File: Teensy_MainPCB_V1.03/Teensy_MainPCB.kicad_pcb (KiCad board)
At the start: 2 copper layers, 141.9 x 100 mm, 68 parts, among them J1 ODO_Right, J10 Sonar_R, J11 Cutter, J12 Sonar_L, J13 P_Right, J14 Buzzer, J15 Button, J16 Power_PCB1, J17 Power_PCB2, J18 Free01_02, J19 P_Left, J2 I2C2_0, J20 Can3, J21 Ser5, J22 FreeA16_A17, J23 ESP RFID1, J24 ESP RFID2, J25 5V IN, J26 ESP32 I2C, J27 ESP32 Sens1, J28 ESP32 FREE, J29 3.3V IN, J3 I2C0_0, J30 I2C1_0, J31 Ser3, J32 ESP32 Sens2, J33 ESP32 I2C/SER, J34 Teensy On/Off, J4 I2C1_1, J5 Bumper, J6 ODO_Left, J7 Motor_Right1, J8 Motor_Left1, J9 Rain, U2 GY-521, U3 Teensy4.1, U4 ESP32-DEVKIT-V1

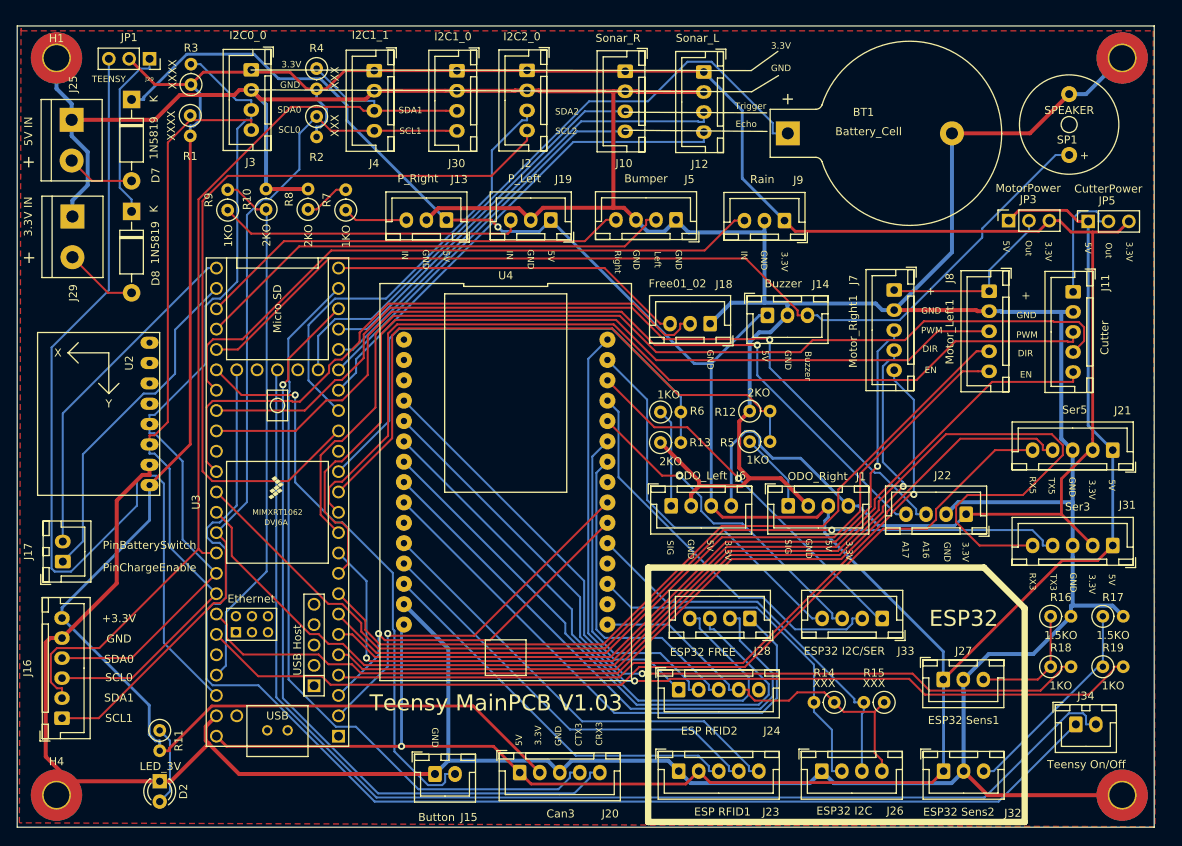
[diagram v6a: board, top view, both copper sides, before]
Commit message: Removed unused
Remove unused Items and sorting new
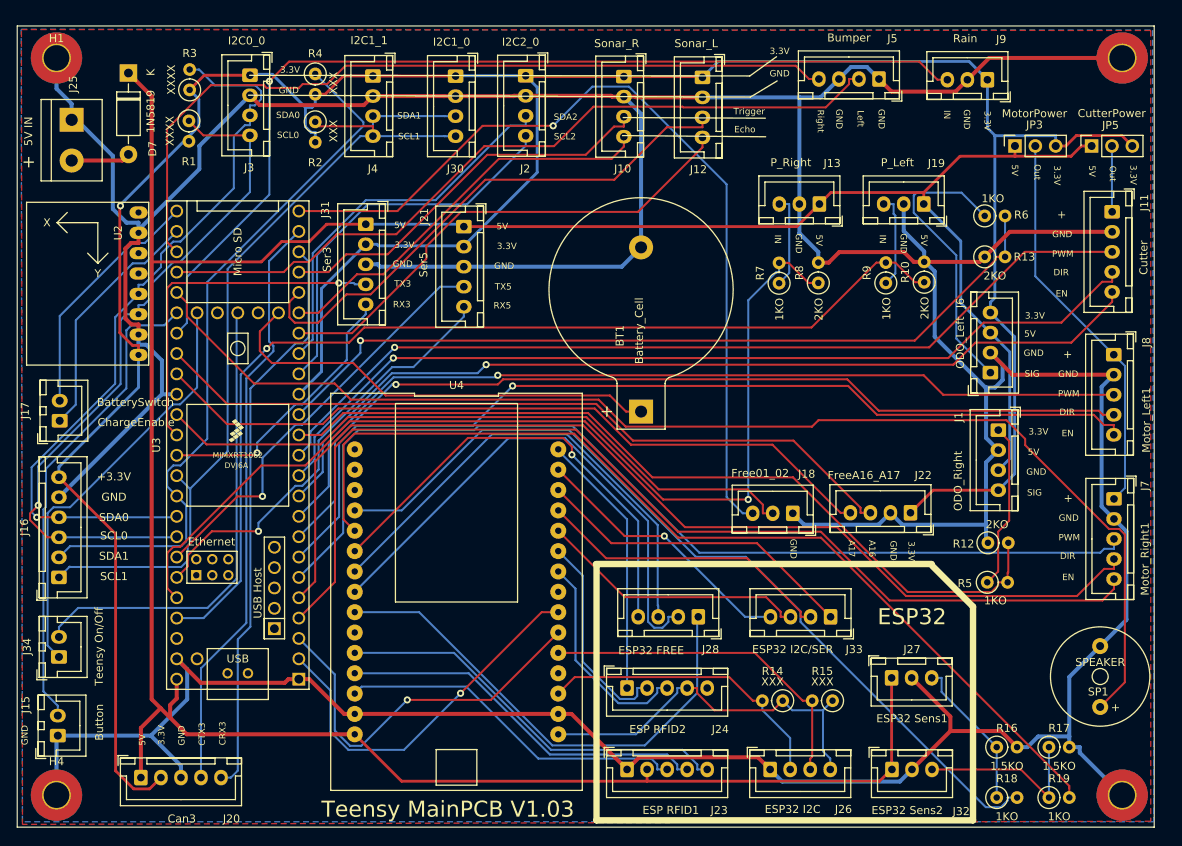
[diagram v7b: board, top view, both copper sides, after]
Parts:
- removed D2: LED_3V, LED_THT:LED_D3.0mm
- removed D8: 1N5819, Diode_THT:D_DO-41_SOD81_P10.16mm_Horizontal
- removed J14: Buzzer, Connector_JST:JST_XH_B3B-XH-A_1x03_P2.50mm_Vertical
- removed J29: 3.3V IN, TerminalBlock:TerminalBlock_bornier-2_P5.08mm
- removed JP1: Jumper_3.3V, Connector_PinSocket_2.54mm:PinSocket_1x03_P2.54mm_Vertical
- removed R11: 100, Resistor_THT:R_Axial_DIN0207_L6.3mm_D2.5mm_P2.54mm_Vertical
- moved J34 127.2 mm to (43.3, 112.8), turned to 90 degrees
- moved J31 101.5 mm to (81.6, 58.8), turned to 270 degrees
- moved J21 85.7 mm to (93.8, 59.0), turned to 270 degrees
- moved R10 82.6 mm to (151.3, 66.0)
- moved R9 82.6 mm to (146.5, 66.1)
- moved SP1 69.0 mm to (173.3, 115.2)
- moved R8 64.3 mm to (138.1, 66.1)
- moved R7 54.8 mm to (133.2, 66.1)
- moved J15 47.3 mm to (43.2, 122.6), turned to 90 degrees
- moved R6 47.3 mm to (158.8, 57.7)
- moved J20 47.3 mm to (53.5, 127.8)
- moved R13 46.6 mm to (158.8, 62.8)
- moved J19 46.6 mm to (151.2, 56.2)
- moved J13 46.6 mm to (138.2, 56.2)
- moved J6 43.2 mm to (159.6, 77.3), turned to 90 degrees
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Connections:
- J24 pad 5: Net-(J24-Pad5) -> (no net)
- R7 pad 2: Net-(R7-Pad2) -> pinPerimeterRight
- R8 pad 1: Net-(R7-Pad2) -> pinPerimeterRight
- U2 pad 5: Net-(U2-Pad5) -> (no net)
- U2 pad 6: Net-(U2-Pad6) -> (no net)
- U2 pad 7: Net-(U2-Pad7) -> GND
- U2 pad 8: Net-(U2-Pad8) -> (no net)
- U3 pad 1: Net-(U3-Pad1) -> GND
- U3 pad 15: Net-(U3-Pad15) -> +3V3
- U3 pad 34: Net-(U3-Pad34) -> GND
- U3 pad 46: Net-(JP1-Pad3) -> (no net)
- U3 pad 49: Net-(U3-Pad49) -> (no net)
- U3 pad 51: Net-(U3-Pad51) -> (no net)
- U3 pad 53: Net-(U3-Pad53) -> (no net)
- U3 pad 55: Net-(U3-Pad55) -> (no net)
- U3 pad 56: Net-(U3-Pad56) -> (no net)
- U3 pad 57: Net-(U3-Pad57) -> (no net)
- U3 pad 58: Net-(U3-Pad58) -> (no net)
- U3 pad 59: Net-(U3-Pad59) -> (no net)
- U3 pad 60: Net-(U3-Pad60) -> (no net)
- U3 pad 61: Net-(U3-Pad61) -> (no net)
- U3 pad 62: Net-(U3-Pad62) -> (no net)
- U3 pad 63: Net-(U3-Pad63) -> (no net)
- U3 pad 64: Net-(U3-Pad64) -> (no net)
- U3 pad 65: Net-(U3-Pad65) -> (no net)
- U3 pad 66: Net-(U3-Pad66) -> (no net)
- U3 pad 67: Net-(U3-Pad67) -> (no net)
- U4 pad 1: Net-(U4-Pad1) -> (no net)
- U4 pad 10: Net-(U4-Pad10) -> (no net)
- U4 pad 17: Net-(U4-Pad17) -> GND
- U4 pad 19: Net-(U4-Pad19) -> (no net)
- U4 pad 2: Net-(U4-Pad2) -> (no net)
- U4 pad 23: Net-(U4-Pad23) -> (no net)
- U4 pad 3: Net-(U4-Pad3) -> (no net)
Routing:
- net pinPerimeterRight: track 0.00 -> 126.7 mm, vias 0 -> 1
- net RX3: track 158.7 -> 34.8 mm, vias 0 -> 1
- net Net-(JP1-Pad3): track 117.0 -> 0.00 mm
- net Net-(J34-Pad1): track 162.5 -> 53.0 mm
- net Net-(J34-Pad2): track 153.9 -> 59.2 mm
- net TX3: track 120.4 -> 43.9 mm
- net TX5: track 121.6 -> 52.6 mm, vias 0 -> 1
- net Free02: track 44.2 -> 108.0 mm, vias 0 -> 1
- net RX5: track 117.4 -> 54.1 mm, vias 0 -> 1
- net pinPerimeterLeft: track 66.6 -> 127.8 mm, vias 0 -> 1
- net SCL2: track 98.7 -> 48.7 mm
- net pinBumperLeft: track 54.5 -> 101.4 mm
- net pinRain: track 79.6 -> 122.8 mm, vias 0 -> 1
- net pinOdometryLeft: track 65.3 -> 102.5 mm, vias 0 -> 1
- net +3V3: track 399.1 -> 363.0 mm, vias 0 -> 1
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- added copper zone on B.Cu, net GND
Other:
- board text added: "BatterySwitch"
- board text added: "ChargeEnable"
- board text removed: "Buzzer"
- board text removed: "J29"
- board text removed: "PinBatterySwitch"
- board text removed: "PinChargeEnable"
- board text removed: "TEENSY"
